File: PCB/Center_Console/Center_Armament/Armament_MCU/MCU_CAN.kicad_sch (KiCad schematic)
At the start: 40 parts, among them J1 Misc_Switch_Panel, J2 AWRS_Panel, J3 SWD Debug, J4 UART SERIAL, J5 J_BUS_IN, J6 J_BUS_OUT, SW1 RESET, U1 STM32F103CBTx, U2 SN65HVD230, U3 AMS1117-3.3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

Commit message: Switch stepper driver DRV8835 → DRV8833PW; rework IRLML2502 symbol
DRV8835 is only available in WSON-12 (bottom-terminated, not inspectable
post-reflow). Replaced throughout with DRV8833PW (HTSSOP-16) which is
already placed in Gauges.kicad_sch as the placeholder.

Library: remove DRV8835 symbol block from OpenSkyhawk.kicad_sym; rework
IRLML2502 symbol body with proper N-channel MOSFET graphical elements
(was a plain rectangle).

Docs: update hardware-standards.md stepper driver section (DRV8833PW,
VINT/VCP/AISEN/FAULT handling); update kicad.md library table; update
Center_Armament.md MCU board component list.

Schematics: KiCad project file and sub-sheets updated from Symbol Editor
session (IRLML2502 symbol refresh across Backlighting and Gauges sheets).
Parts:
- C12, C15: footprint (none) -> Capacitor_SMD:C_0805_2012Metric
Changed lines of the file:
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@@
 			)
 		)
-		(property "Footprint" ""
+		(property "Footprint" "Capacitor_SMD:C_0805_2012Metric"
 			(at 240.9952 130.81 0)
 			(hide yes)
@@
 			)
 		)
-		(property "Footprint" ""
+		(property "Footprint" "Capacitor_SMD:C_0805_2012Metric"
 			(at 216.8652 152.4 0)
 			(hide yes)

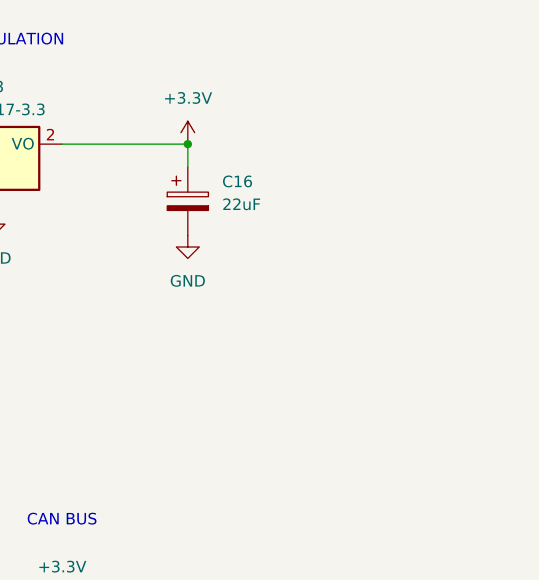
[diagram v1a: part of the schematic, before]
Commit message: Add AWRS_Panel schematic; refresh symbol caches
AWRS_Panel: 2-sheet hierarchical breakout board schematic.
Root sheet: ADS1115 @ 0x48 (ADDR→GND), three RC-filtered analog inputs
(A0=QTY, A1=DROP INTVL, A2=MODE SEL), 1kΩ+100nF per input, three 4-pin
JST-XH pot connectors (J1/J3/J5), 6-pin JST-XH MCU harness (J2), VDD
decoupling (C1 100nF + C2 10µF), status LED (D1+R22), PWR_FLAGs.
Backlighting sheet: 3 LED strings × 5 LEDs, 3×120Ω resistors, 2-pin
Mini-Fit Jr (J_LED). Controls sheet: placeholder — panel-mounted switch
types and position counts deferred until extracted from DCS sim.

MCU_CAN.kicad_sch, Misc_Switch_Panel.kicad_sch: symbol cache refresh
from IRLML2502 library rework.
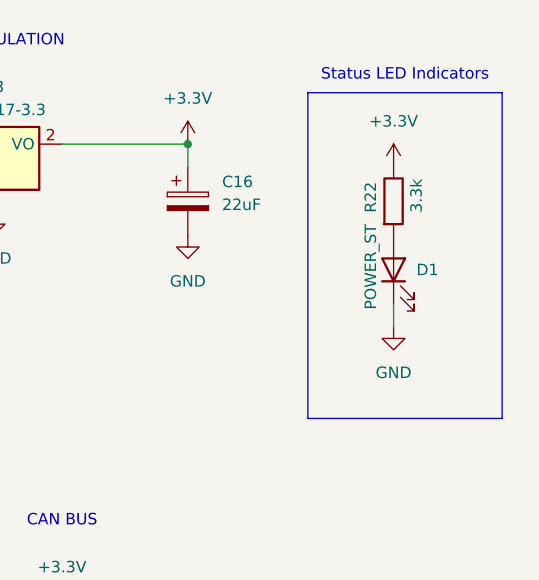
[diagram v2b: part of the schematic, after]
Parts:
- added D1: POWER_ST, LED_SMD:LED_0805_2012Metric, symbol Device:LED
- added R22: 3.3k, Resistor_SMD:R_0805_2012Metric, symbol Device:R
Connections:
- net +3.3V: now also R22.1
- net GND: now also D1.1 (K)
- new net: D1.2 (A), R22.2
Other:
- note added: "Status LED Indicators"

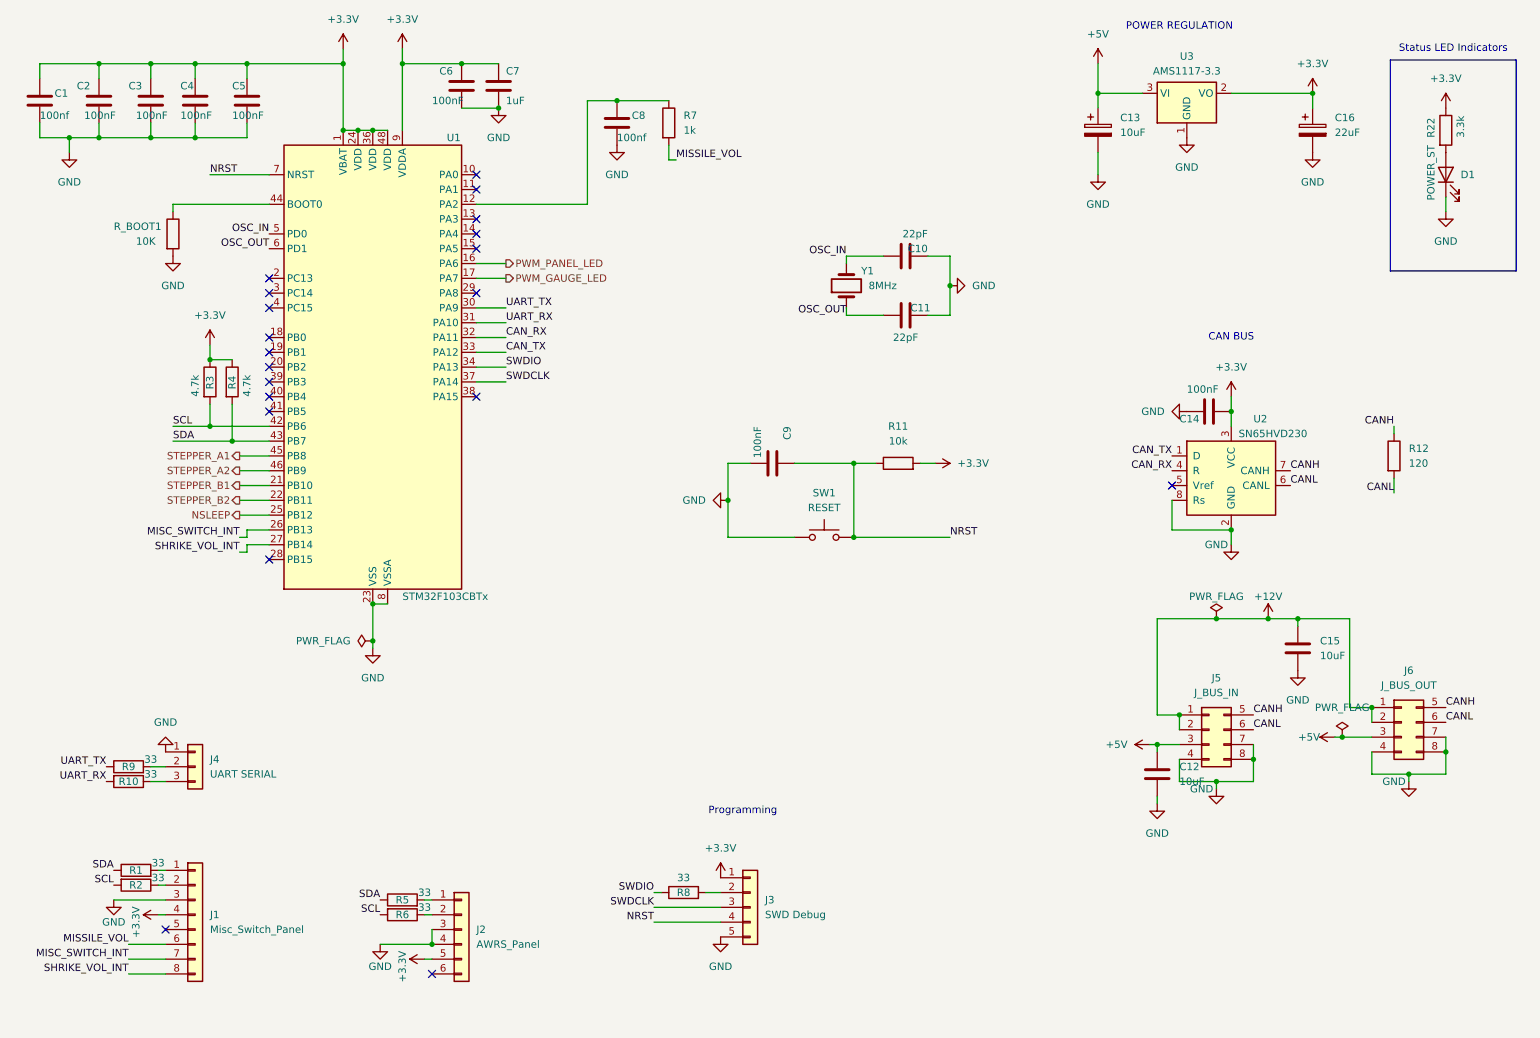
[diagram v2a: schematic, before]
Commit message: pcb: update Armament MCU status LED wiring
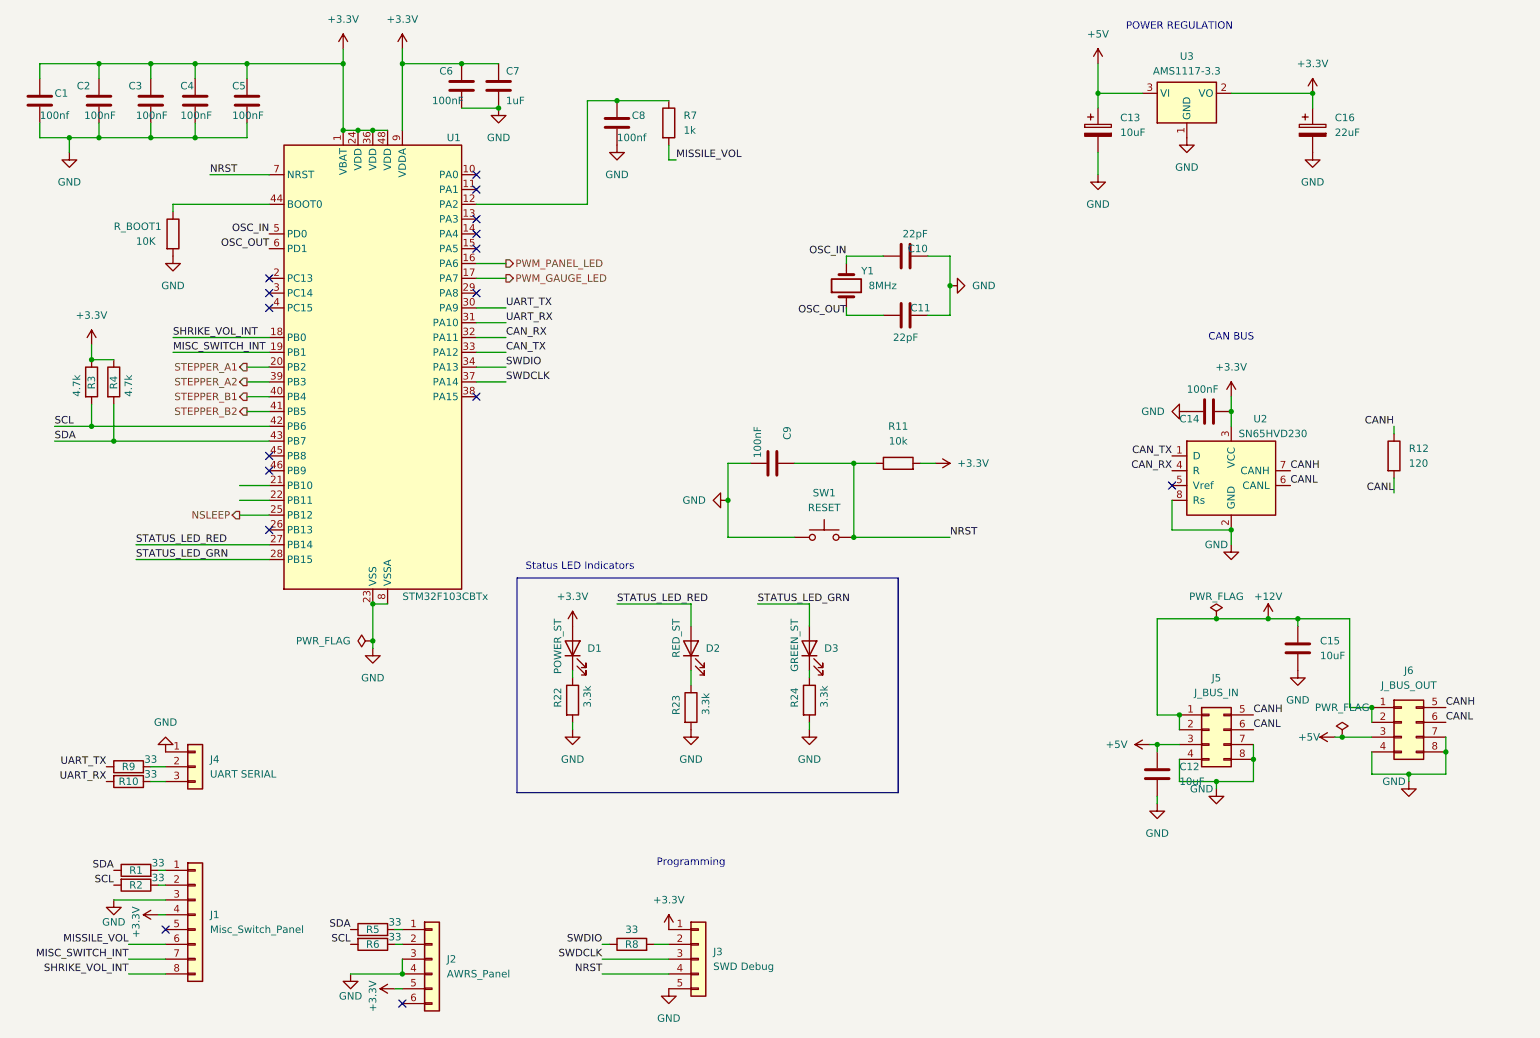
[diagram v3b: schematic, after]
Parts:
- added D2: RED_ST, LED_SMD:LED_0805_2012Metric, symbol Device:LED
- added D3: GREEN_ST, LED_SMD:LED_0805_2012Metric, symbol Device:LED
- added R23, R24: 3.3k, Resistor_SMD:R_0805_2012Metric, symbol Device:R
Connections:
- net +3.3V: now also D1.2 (A); no longer R22.1
- net GND: now also R22.2, R23.2, R24.2; no longer D1.1 (K)
- net MISC_SWITCH_INT: now also U1.19 (PB1); no longer U1.26 (PB13)
- net SHRIKE_VOL_INT: now also U1.18 (PB0); no longer U1.27 (PB14)
- net STEPPER_A1: now also U1.20 (PB2); no longer U1.45 (PB8)
- net STEPPER_A2: now also U1.39 (PB3); no longer U1.46 (PB9)
- net STEPPER_B1: now also U1.40 (PB4); no longer U1.21 (PB10)
- net STEPPER_B2: now also U1.41 (PB5); no longer U1.22 (PB11)
- net STATUS_LED_GRN: now reaches U1.28 (PB15)
- net STATUS_LED_GRN: now also D3.2 (A)
- new net: D2.1 (K), R23.1
- new net: D3.1 (K), R24.1
- new net: D1.1 (K), R22.1
- new net STATUS_LED_RED: D2.2 (A), U1.27 (PB14)
- no-connect marks 20 -> 16
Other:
- moved on the sheet: D1, J2, J3, R3, R4, R5, R6, R8
